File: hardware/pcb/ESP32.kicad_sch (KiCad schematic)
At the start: 9 parts, among them SW1 BOOT, SW1 EN, U4 ESP32-S3-WROOM-1

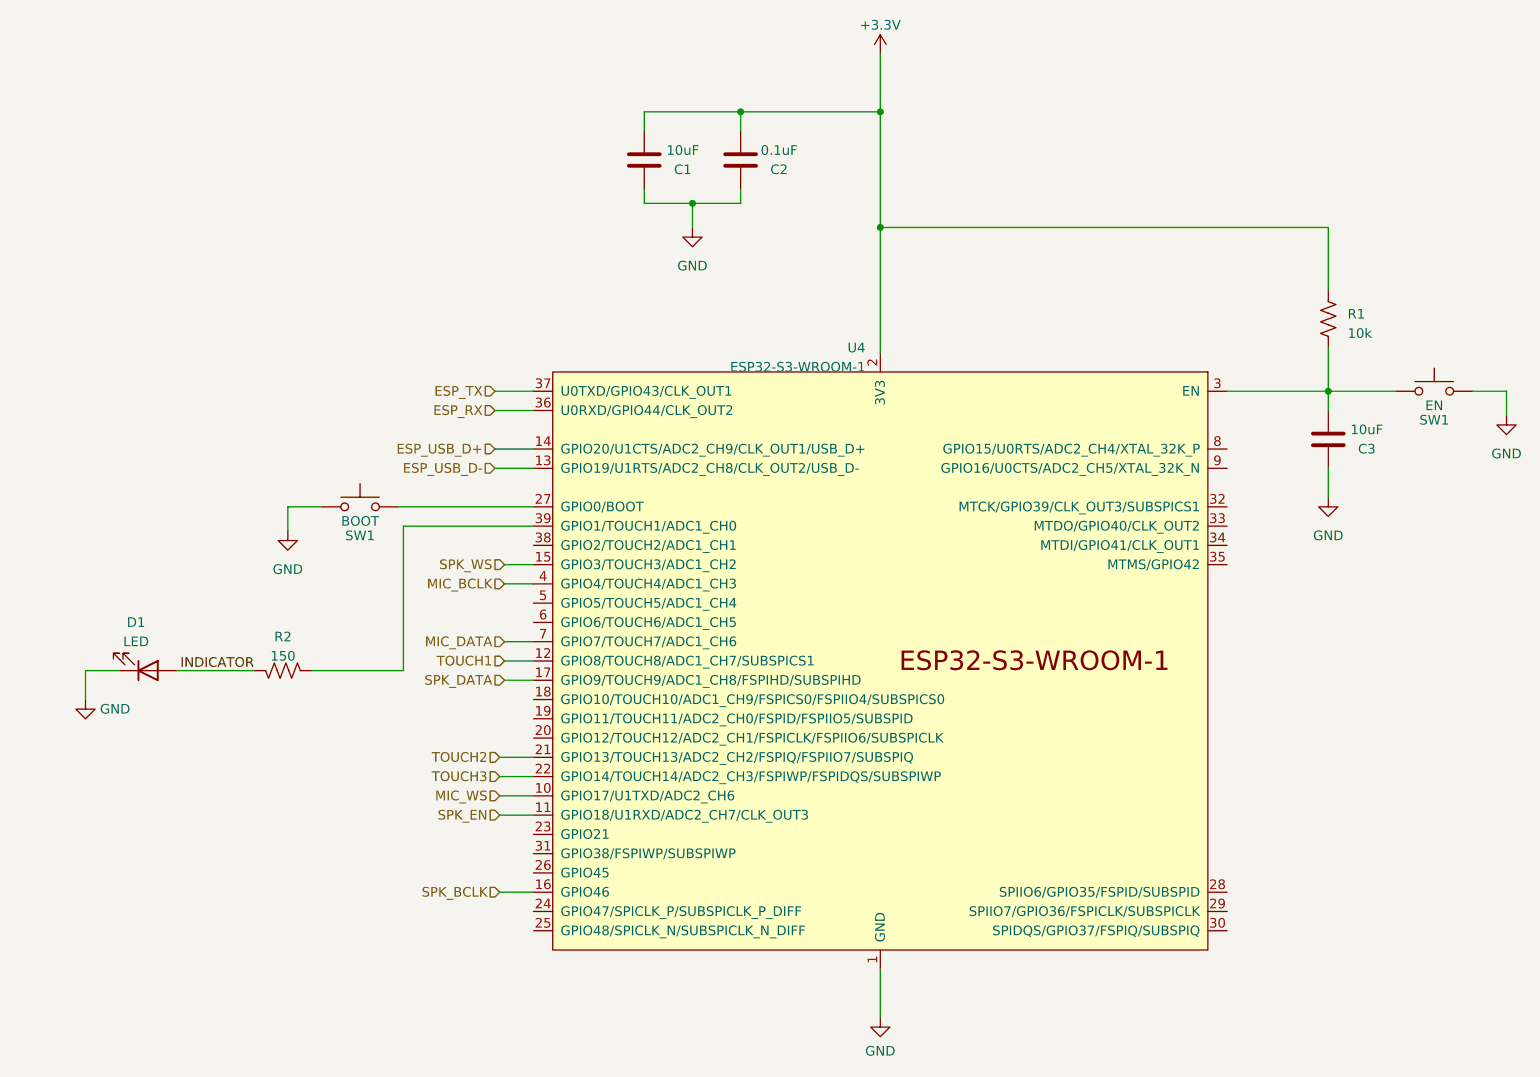
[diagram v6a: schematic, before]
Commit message: Use noncritical GPIO pins for I2S peripherals
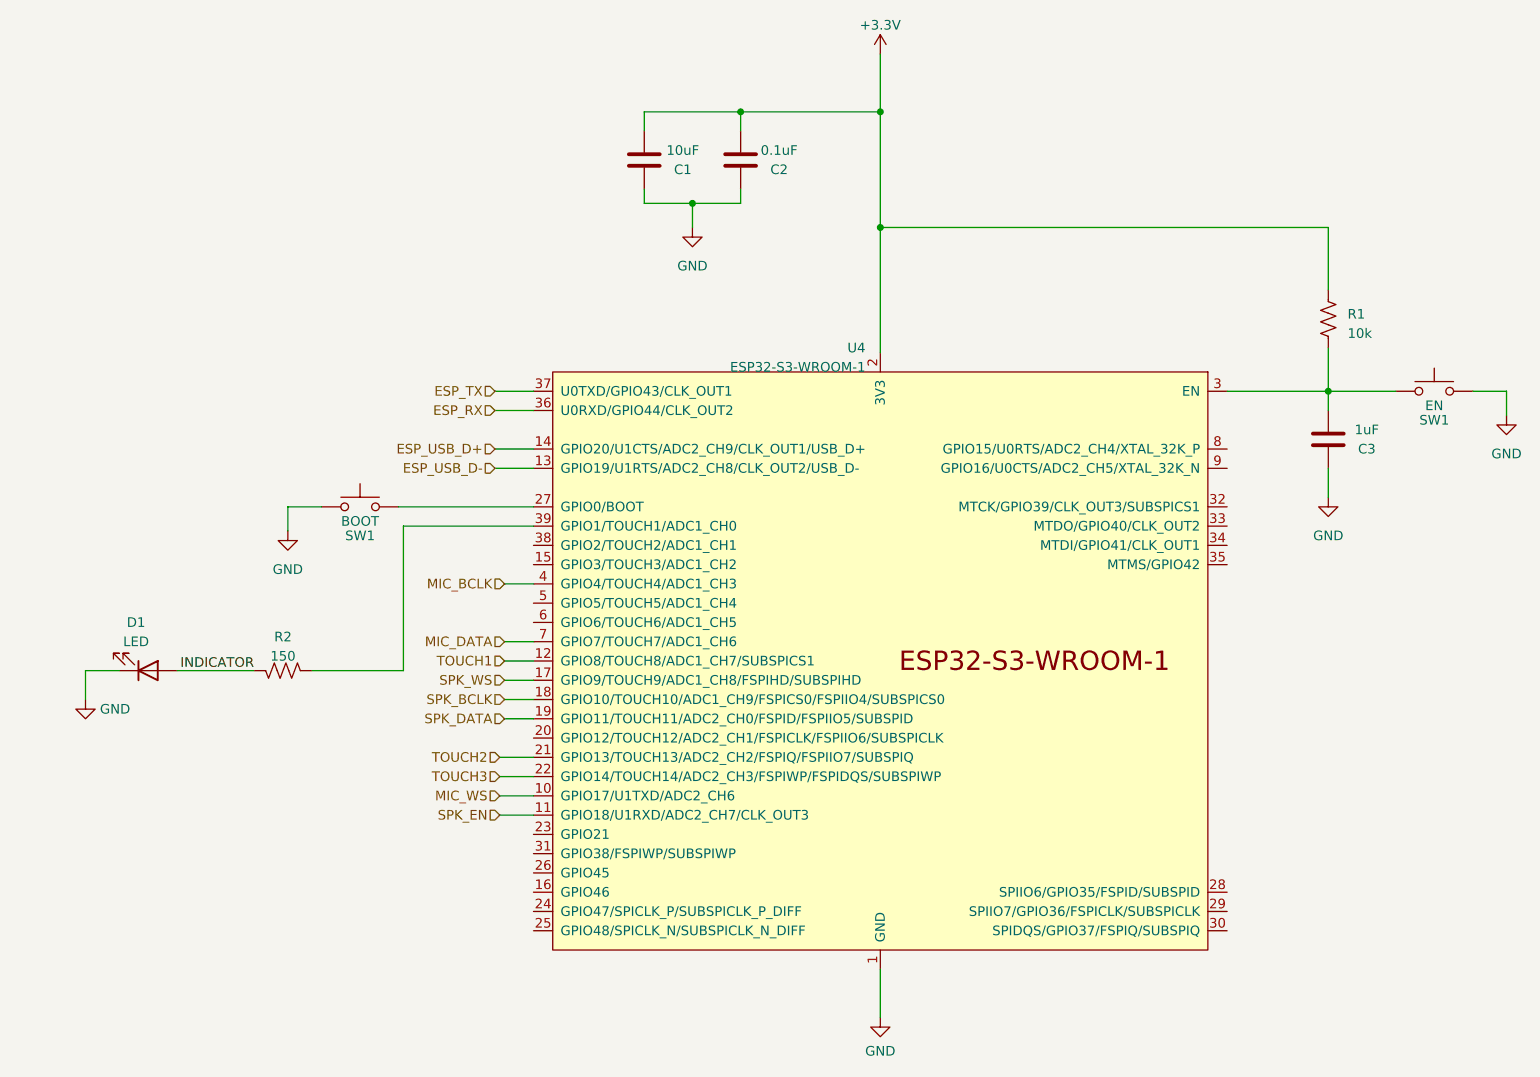
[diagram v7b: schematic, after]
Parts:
- C3: value 10uF -> 1uF
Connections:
- net SPK_BCLK: now also U4.18 (GPIO10/TOUCH10/ADC1_CH9/FSPICS0/FSPIIO4/SUBSPICS0); no longer U4.16 (GPIO46)
- net SPK_DATA: now also U4.19 (GPIO11/TOUCH11/ADC2_CH0/FSPID/FSPIIO5/SUBSPID); no longer U4.17 (GPIO9/TOUCH9/ADC1_CH8/FSPIHD/SUBSPIHD)
- net SPK_WS: now also U4.17 (GPIO9/TOUCH9/ADC1_CH8/FSPIHD/SUBSPIHD); no longer U4.15 (GPIO3/TOUCH3/ADC1_CH2)
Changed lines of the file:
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@@
-    (stroke (width 0) (type default))
-  )
-  (wire (pts (xy 107.95 135.255) (xy 112.395 135.255))
     (stroke (width 0) (type default))
   )
@@
     (stroke (width 0) (type default))
   )
+  (wire (pts (xy 217.17 55.88) (xy 217.17 47.625))
+    (stroke (width 0) (type default))
+  )
+  (wire (pts (xy 75.565 106.045) (xy 65.405 106.045))
+    (stroke (width 0) (type default))
+  )
+  (wire (pts (xy 158.115 145.415) (xy 158.115 151.765))
+    (stroke (width 0) (type default))
+  )
+  (wire (pts (xy 127 44.45) (xy 133.35 44.45))
+    (stroke (width 0) (type default))
+  )
+  (wire (pts (xy 108.585 112.395) (xy 112.395 112.395))
+    (stroke (width 0) (type default))
+  )
+  (wire (pts (xy 107.95 120.015) (xy 112.395 120.015))
+    (stroke (width 0) (type default))
+  )
   (wire (pts (xy 108.585 107.315) (xy 112.395 107.315))
     (stroke (width 0) (type default))
   )
-  (wire (pts (xy 217.17 55.88) (xy 217.17 47.625))
-    (stroke (width 0) (type default))
-  )
-  (wire (pts (xy 75.565 106.045) (xy 65.405 106.045))
-    (stroke (width 0) (type default))
-  )
-  (wire (pts (xy 158.115 145.415) (xy 158.115 151.765))
-    (stroke (width 0) (type default))
-  )
-  (wire (pts (xy 127 44.45) (xy 133.35 44.45))
-    (stroke (width 0) (type default))
-  )
-  (wire (pts (xy 107.95 120.015) (xy 112.395 120.015))
-    (stroke (width 0) (type default))
-  )
   (wire (pts (xy 203.835 69.215) (xy 217.17 69.215))
     (stroke (width 0) (type default))
@@
     (stroke (width 0) (type default))
   )
+  (wire (pts (xy 108.585 109.855) (xy 112.395 109.855))
+    (stroke (width 0) (type default))
+  )
   (wire (pts (xy 95.25 86.995) (xy 95.25 106.045))
     (stroke (width 0) (type default))
@@
   )
   (wire (pts (xy 158.115 32.385) (xy 158.115 47.625))
-    (stroke (width 0) (type default))
-  )
-  (wire (pts (xy 108.585 92.075) (xy 112.395 92.075))
     (stroke (width 0) (type default))
   )
@@
     (effects (font (size 1.27 1.27)) (justify right))
   )
-  (hierarchical_label "SPK_DATA" (shape input) (at 108.585 107.315 180) (fields_autoplaced)
+  (hierarchical_label "SPK_DATA" (shape input) (at 108.585 112.395 180) (fields_autoplaced)
     (effects (font (size 1.27 1.27)) (justify right))
   )
@@
     (effects (font (size 1.27 1.27)) (justify right))
   )
-  (hierarchical_label "SPK_WS" (shape input) (at 108.585 92.075 180) (fields_autoplaced)
+  (hierarchical_label "SPK_WS" (shape input) (at 108.585 107.315 180) (fields_autoplaced)
     (effects (font (size 1.27 1.27)) (justify right))
   )
@@
     (effects (font (size 1.27 1.27)) (justify right))
   )
-  (hierarchical_label "SPK_BCLK" (shape input) (at 107.95 135.255 180) (fields_autoplaced)
+  (hierarchical_label "SPK_BCLK" (shape input) (at 108.585 109.855 180) (fields_autoplaced)
     (effects (font (size 1.27 1.27)) (justify right))
   )
@@
       (effects (font (size 1.27 1.27)))
     )
-    (property "Value" "10uF" (at 222.25 74.295 0)
-      (effects (font (size 1.27 1.27)))
-    )
+    (property "Value" "1uF" (at 222.25 74.295 0)
+      (effects (font (size 1.27 1.27)))
+    )
